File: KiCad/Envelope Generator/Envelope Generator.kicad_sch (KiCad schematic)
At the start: 56 parts, among them J1 Screw_Terminal_01x03, J2 Screw_Terminal_01x03, U1 TL074, U2 TL074, U3 TL074

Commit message: oscillator pcb layout done
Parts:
- C2: footprint Capacitor_THT:C_Rect_L31.5mm_W20.0mm_P27.50mm_MKS4 -> Capacitor_THT:C_Rect_L7.2mm_W4.5mm_P5.00mm
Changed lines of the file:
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@@
 			)
 		)
-		(property "Footprint" "Capacitor_THT:C_Rect_L31.5mm_W20.0mm_P27.50mm_MKS4"
+		(property "Footprint" "Capacitor_THT:C_Rect_L7.2mm_W4.5mm_P5.00mm"
 			(at 48.26 110.7948 0)
 			(hide yes)

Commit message: added mounting holes to schematics, adjusted board sizes
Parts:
- added H1, H2, H3, H4: MountingHole, MountingHole:MountingHole_3.2mm_M3, symbol Mechanical:MountingHole

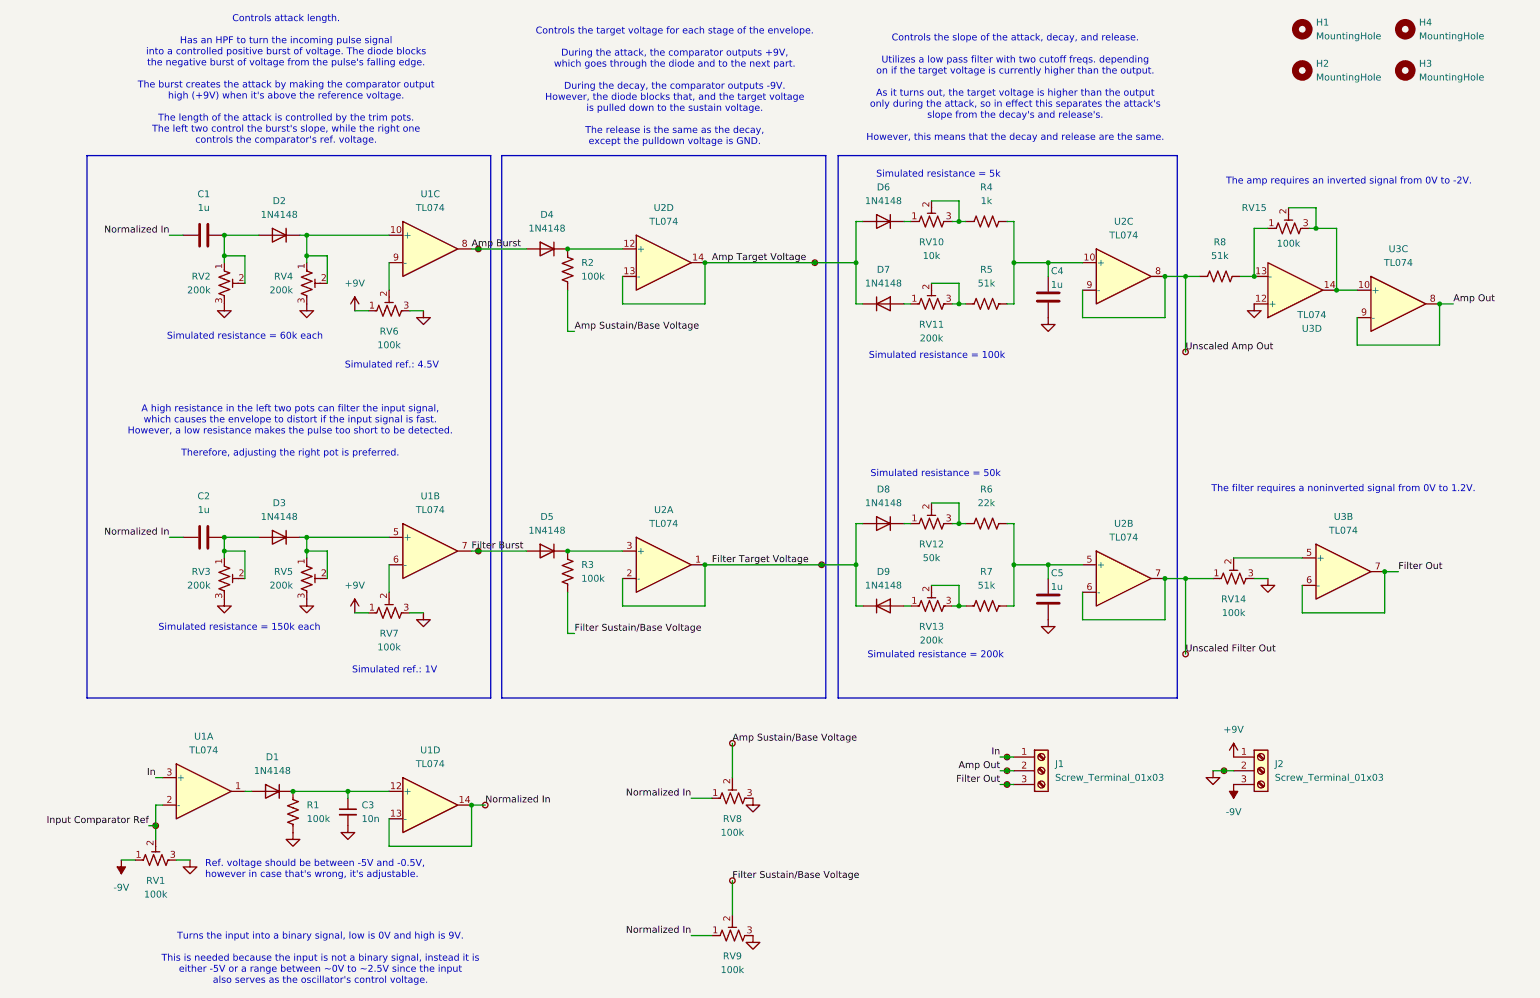
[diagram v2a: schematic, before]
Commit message: envelope generator pcb layout done
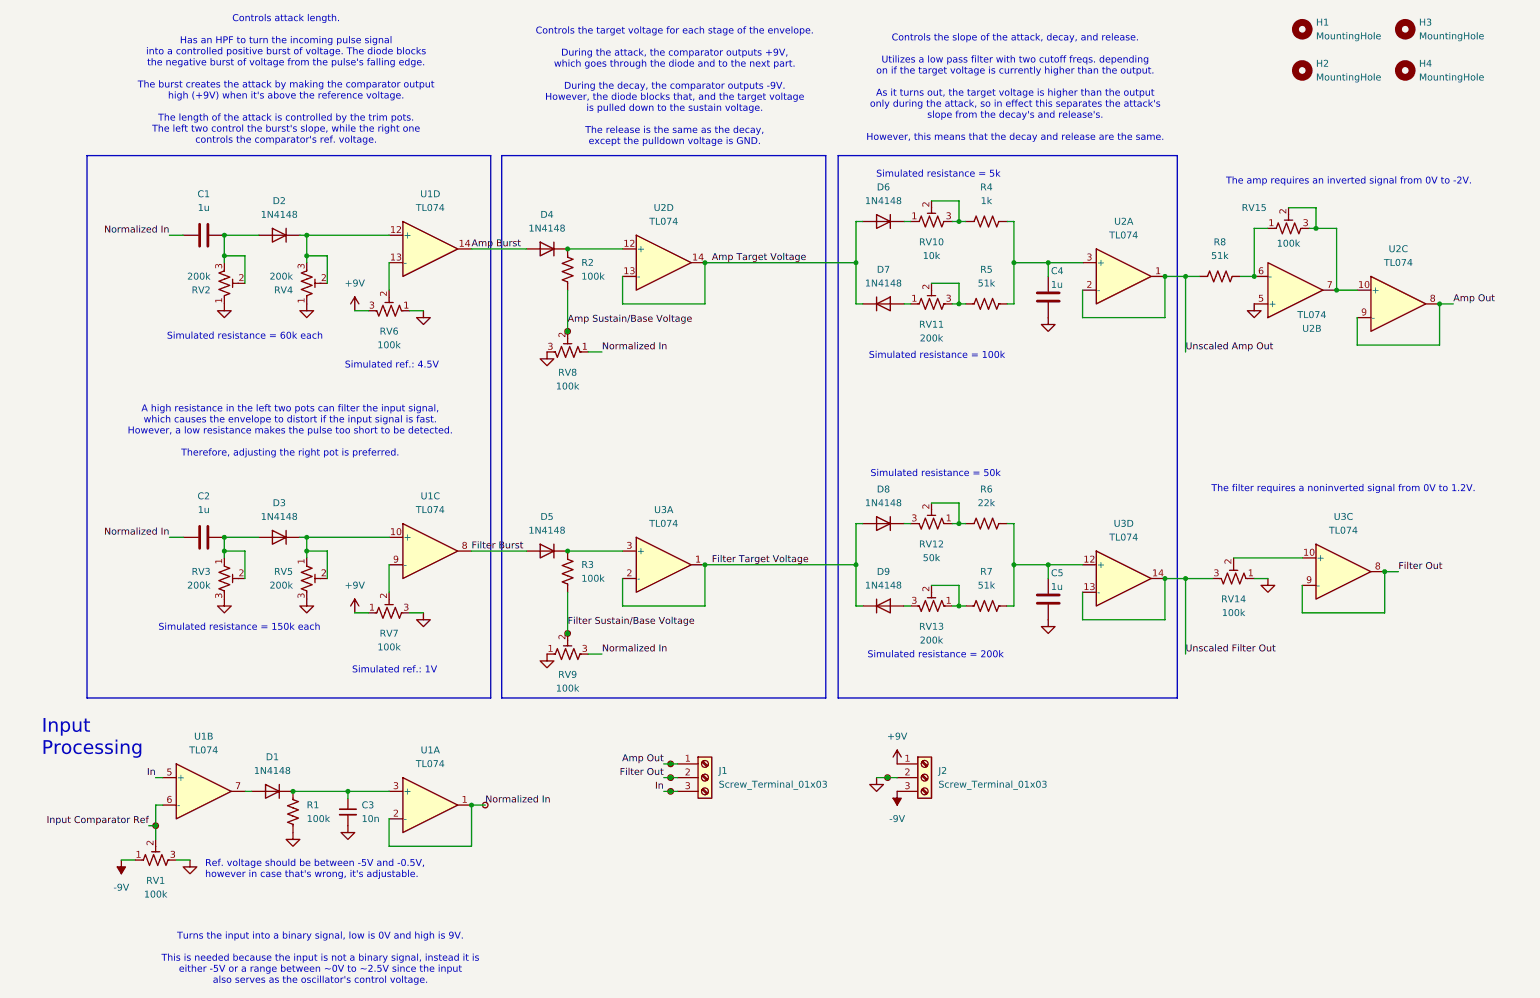
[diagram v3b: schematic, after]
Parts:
- removed TP12, TP13, TP2, TP3, TP7, TP8: TestPoint_Small, TestPoint:TestPoint_Keystone_5000-5004_Miniature, symbol Connector:TestPoint_Small
- renumbered H4 to H3, H3 to H4, TP14 to TP12, TP9 to TP7, TP10 to TP8, TP11 to TP9, U3 to U2, U2 to U3
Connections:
- net +9V: now also RV6.3; no longer RV6.1
- net Amp Burst: now also U1.14; no longer U1.8
- net Amp Out: now also J1.1 (Pin_1), TP7.1; no longer J1.2 (Pin_2), TP8.1
- net Filter Burst: now also U1.8; no longer U1.7
- net Filter Out: now also J1.2 (Pin_2), TP8.1, U3.8, U3.9 (-); no longer J1.3 (Pin_3), TP9.1, U3.6 (-), U3.7
- net GND: now also RV14.1, RV2.1, RV4.1, RV6.1, RV9.1, U2.5 (+); no longer RV14.3, RV2.3, RV4.3, RV6.3, RV9.3, U2.12 (+)
- net In: now also J1.3 (Pin_3), TP9.1, U1.5 (+); no longer J1.1 (Pin_1), TP7.1, U1.3 (+)
- net Input Comparator Ref: now also U1.6 (-); no longer U1.2 (-)
- net Normalized In: now also RV9.3, U1.1, U1.2 (-); no longer RV9.1, U1.13 (-), U1.14
- net Unscaled Amp Out: now also U2.1, U2.2 (-); no longer U2.8, U2.9 (-)
- net Unscaled Filter Out: now also RV14.3, U3.13 (-), U3.14; no longer RV14.1, U3.6 (-), U3.7
- net at C4.2, R4.2, R5.2: now also U2.3 (+); no longer U2.10 (+)
- net at RV14.2: now also U3.10 (+); no longer U3.5 (+)
- net at RV7.2: now also U1.9 (-); no longer U1.6 (-)
- net at C5.2, R6.2, R7.2: now also U3.12 (+); no longer U3.5 (+)
- net at R6.1, RV12.2: now also RV12.1; no longer RV12.3
- net at D2.1 (K), RV4.2: now also RV4.3, U1.12 (+); no longer RV4.1, U1.10 (+)
- net at C3.1, D1.1 (K), R1.1: now also U1.3 (+); no longer U1.12 (+)
- net at C1.2, D2.2 (A), RV2.2: now also RV2.3; no longer RV2.1
- net at D3.1 (K), RV5.1, RV5.2: now also U1.10 (+); no longer U1.5 (+)
- net at D8.1 (K): now also RV12.3; no longer RV12.1
- net at D1.2 (A): now also U1.7; no longer U1.1
- net at D9.2 (A): now also RV13.3; no longer RV13.1
- net at R8.2, RV15.1: now also U2.6 (-); no longer U2.13 (-)
- net at RV6.2: now also U1.13 (-); no longer U1.9 (-)
- net at R7.1, RV13.2: now also RV13.1; no longer RV13.3
- net at RV15.2, RV15.3, U2.10 (+): now also U2.7; no longer U2.14
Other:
- note added: "Input Processing"
- moved on the sheet: J1, J2, RV12, RV13, RV14, RV6, RV8, RV9

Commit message: preparation to merge project back into one board
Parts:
- C1, C2, C4, C5: KiLib_Generator (none) -> capacitor/THT/other
- C3, R1, R2, R3, R4, R5, R6, R7, R8: KiLib_Generator (none) -> SMD_2terminal_chip_molded
- D1, D2, D3, D4, D5, D6, D7, D8, D9: KiLib_Generator (none) -> diode/THT
- H1, H2, H3, H4: KiLib_Generator (none) -> mounting_hardware/mounting_hole
- RV1, RV10, RV11, RV12, RV13, RV14, RV15, RV2, RV3, RV4, RV5, RV6, RV7, RV8, RV9: KiLib_Generator (none) -> potentiometer/THT
- U1, U2, U3: KiLib_Generator (none) -> package/DIP/legacy
